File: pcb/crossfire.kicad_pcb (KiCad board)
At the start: 4 copper layers, 100 x 54 mm, 92 parts, among them J1 SWD+UART, J2 USB_A, J3 USB_A, J4 USB_A, J5 USB_A, J6 USB-C, SW1 BOOT, SW2 RESET, SW3 USER, U1 RP2350A, U10 TPS2065C, U11 USBLC6-2SC6, U12 USBLC6-2SC6, U14 AP63203WU, U2 W25Q128JVS, U3 USB2514B, U4 TPS2065C, U5 USBLC6-2SC6, U6 TPS2065C, U7 USBLC6-2SC6, U8 TPS2065C, U9 USBLC6-2SC6, Y1 12MHz, Y2 24MHz

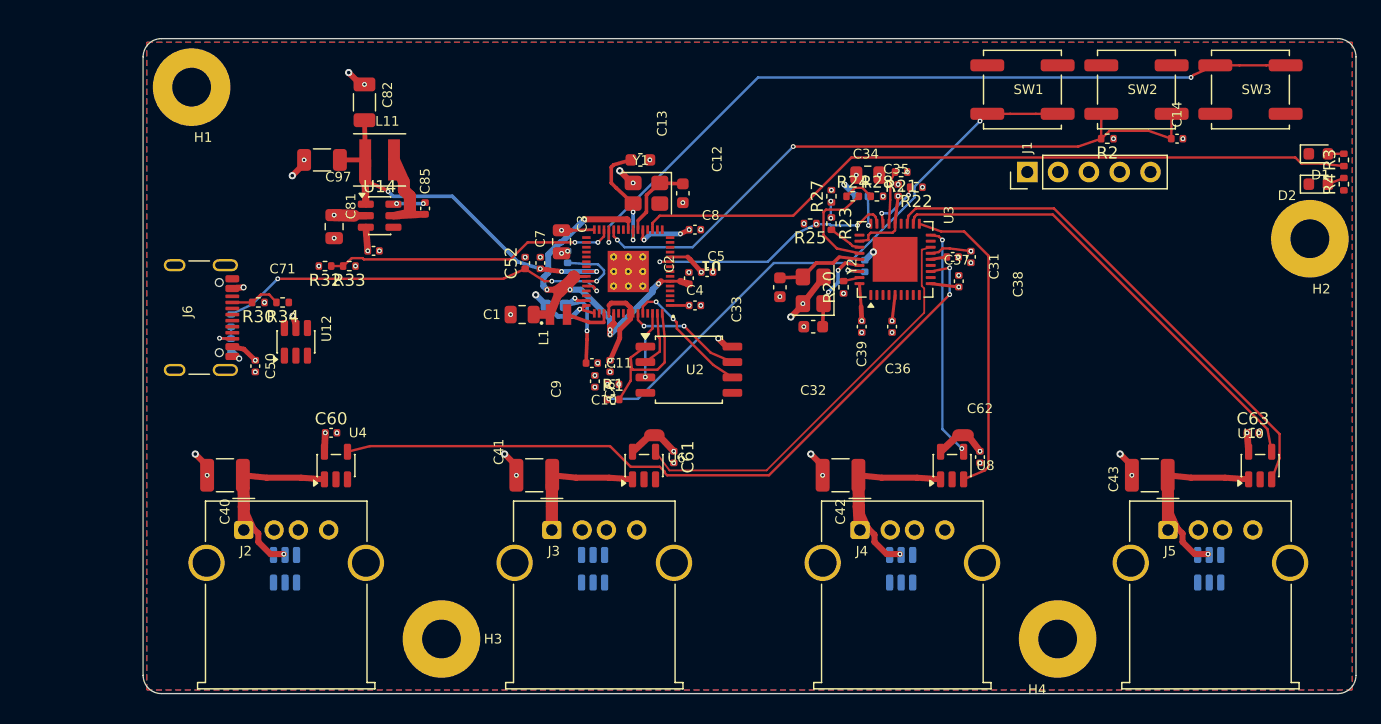
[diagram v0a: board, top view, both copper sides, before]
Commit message: hand layout and routing of the single-input board
All six pairs routed, the port power and fault lines moved to the back,
the crystal above the processor, a 100 nF on DVDD pin 23 added to the
schematic as C15. Rules check: three shorts on HUB_RESET's back-layer run
and three clearances still to clear; thirteen connections still open.

Co-Authored-By: Claude Fable 5.1 <noreply@anthropic.com>
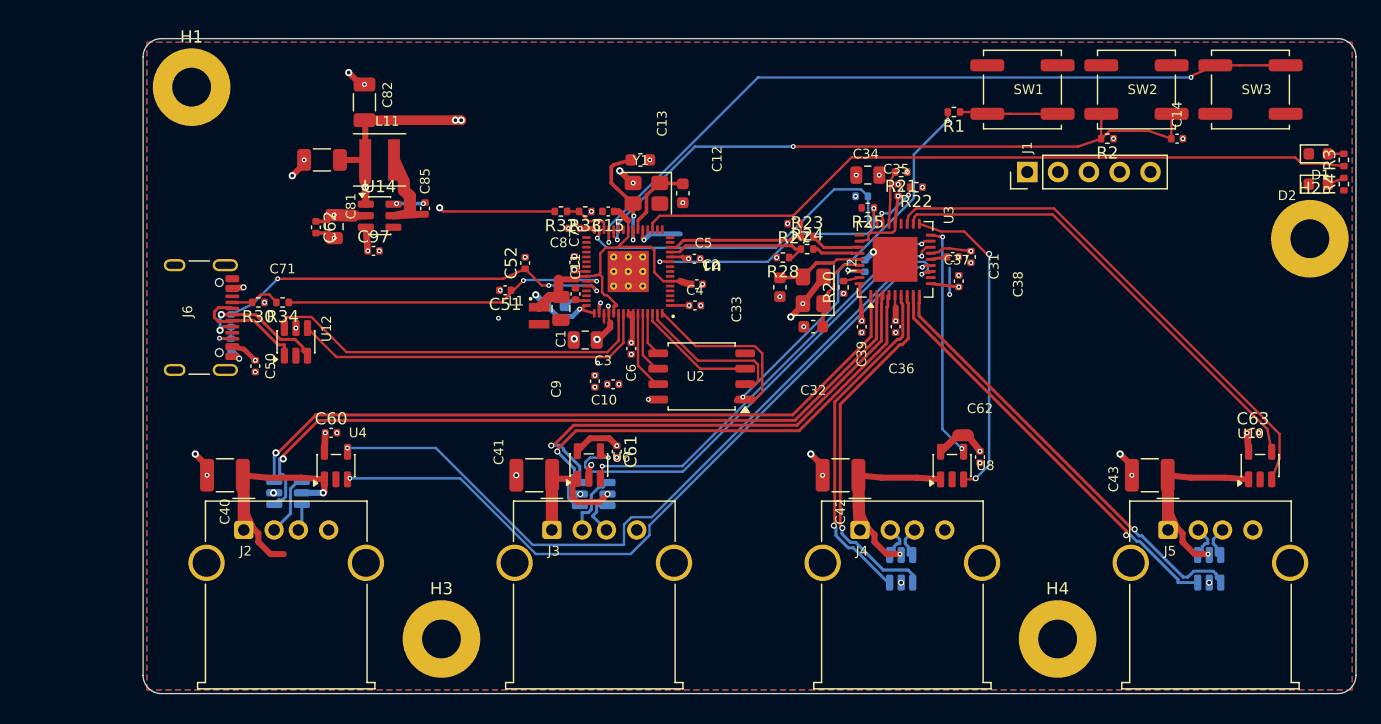
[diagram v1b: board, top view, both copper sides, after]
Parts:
- added C15: 100n, Capacitor_SMD:C_0402_1005Metric, F.Cu at (136.8, 59.2)
- added C62: 100n, Capacitor_SMD:C_0402_1005Metric, F.Cu at (112.8, 60.5)
- C51: footprint C_0402_1005Metric -> Capacitor_SMD:C_0402_1005Metric; moved to F.Cu
- C52, C60, C61, C63, C97: footprint C_0402_1005Metric -> Capacitor_SMD:C_0402_1005Metric
- H1, H2, H3, H4: footprint MountingHole_3.2mm_M3_Pad -> MountingHole:MountingHole_3.2mm_M3_Pad
- R1, R2, R20, R21, R22, R23, R24, R25, R26, R27, R28, R3, R30, R31, R32, R33, R34, R35, R4: footprint R_0402_1005Metric -> Resistor_SMD:R_0402_1005Metric
- U14: footprint TSOT-23-6 -> Package_TO_SOT_SMD:TSOT-23-6
- moved R1 36.8 mm to (165.3, 51.0), turned to 180 degrees
- moved R32 20.0 mm to (132.9, 59.2)
- moved R33 20.0 mm to (134.9, 59.2)
- moved C8 9.95 mm to (134.1, 60.6), turned to 180 degrees
- moved R28 9.25 mm to (151.2, 63.0), turned to 180 degrees
- moved C3 8.33 mm to (134.9, 69.8), turned to 180 degrees
- moved U5 6.26 mm to (110.5, 82.5), turned to 0 degrees
- moved U7 6.16 mm to (135.7, 82.5), turned to 0 degrees
- moved C11 5.86 mm to (134.2, 66.0), turned to 90 degrees
- moved C51 5.84 mm to (128.3, 65.8), turned to 180 degrees
- moved R24 5.74 mm to (153.2, 62.4)
- moved R25 4.92 mm to (158.2, 59.0)
- moved C61 4.72 mm to (137.6, 79.0)
- moved U6 4.55 mm to (135.2, 80.2)
- moved R27 3.83 mm to (152.2, 60.2), turned to 180 degrees
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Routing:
- net /P1_D+: track 0.00 -> 61.8 mm, vias 0 -> 1
- net /P1_OC: track 0.00 -> 61.0 mm, vias 0 -> 2
- net /P1_D-: track 0.00 -> 58.9 mm, vias 0 -> 1
- net /P2_D+: track 0.00 -> 41.0 mm, vias 0 -> 1
- net Net-(R1-Pad1): track 47.4 -> 8.10 mm, vias 2 -> 0
- net /P2_D-: track 0.00 -> 39.2 mm, vias 0 -> 1
- net /P4_D+: track 0.00 -> 36.4 mm, vias 0 -> 1
- net /P2_OC: track 0.00 -> 35.9 mm, vias 0 -> 2
- net /P4_D-: track 0.00 -> 34.8 mm, vias 0 -> 1
- net Net-(U1-~{QSPI_SS}): track 13.2 -> 45.8 mm, vias 0 -> 2
- net /USB_D-: track 0.00 -> 32.2 mm
- net /USB_D+: track 0.00 -> 30.5 mm
- net /P3_D+: track 0.00 -> 30.1 mm, vias 0 -> 1
- net /P3_D-: track 0.00 -> 28.5 mm, vias 0 -> 1
- net /HUB_VBUS_DET: track 2.64 -> 28.3 mm, vias 1 -> 2
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
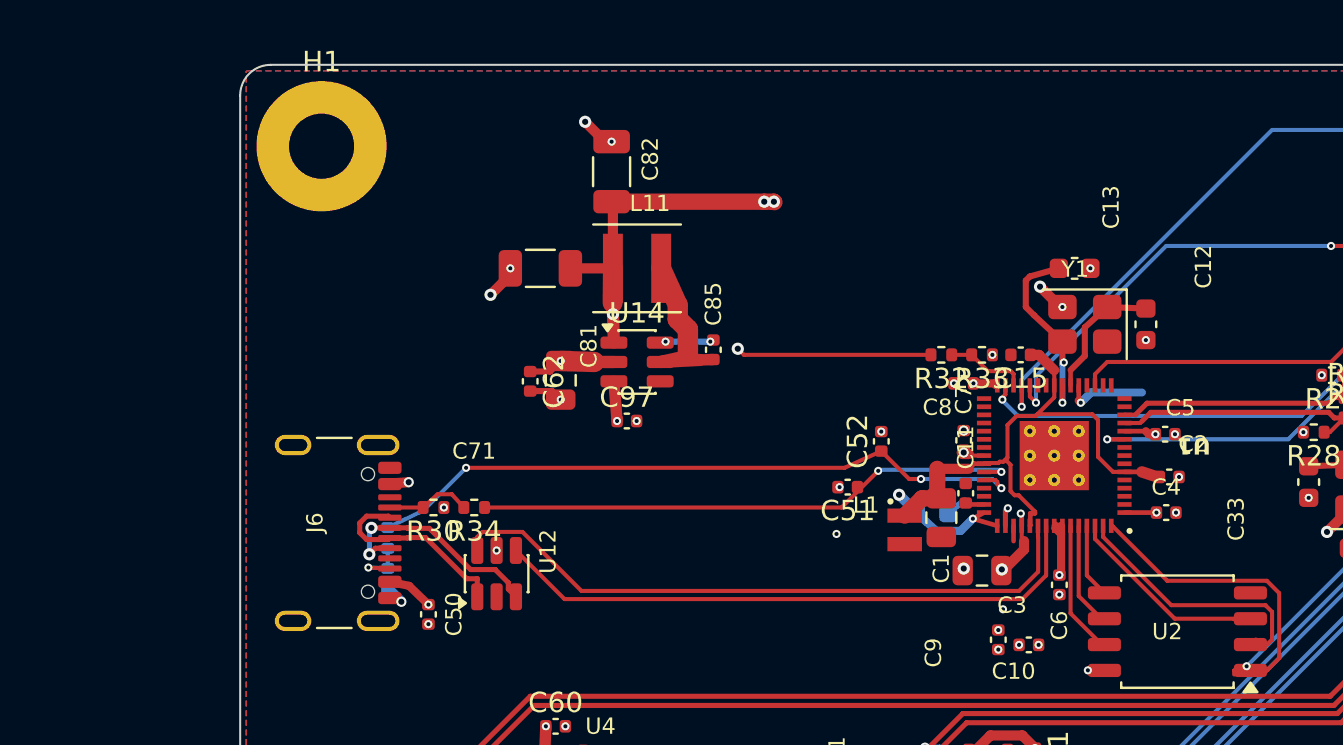
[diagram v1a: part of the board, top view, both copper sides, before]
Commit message: take the processor's regulator parts from the vendor's reference design
4.7 uF in 0402 on VREG_VIN and on the core rail, where this board had 10 uF
and 4.7 uF in 0805, and a 33 ohm / 4.7 uF filter on VREG_AVDD, which it
did not have at all. The crystal's load capacitors go to 0402 and the
3.3 V buck's capacitors to 0603. Footprints are swapped on the board in
place so the layout stands; R5 and C16 are parked outside the left edge.

Co-Authored-By: Claude Fable 5.1 <noreply@anthropic.com>
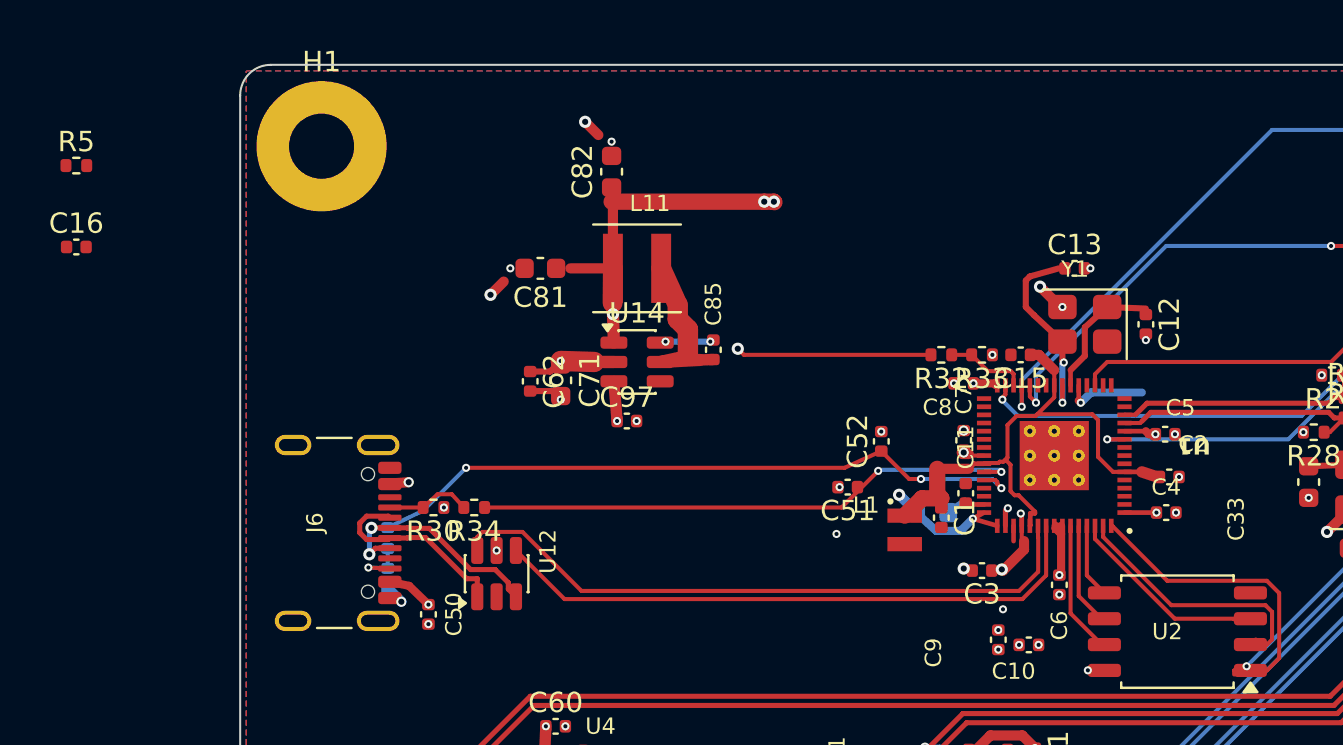
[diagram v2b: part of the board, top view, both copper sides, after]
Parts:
- added C16: 4u7, C_0402_1005Metric, F.Cu at (90.5, 54.0)
- added R5: 33R, R_0402_1005Metric, F.Cu at (90.5, 50.0)
- C1: footprint Capacitor_SMD:C_0805_2012Metric -> C_0402_1005Metric
- C12, C13: footprint Capacitor_SMD:C_0603_1608Metric -> C_0402_1005Metric
- C3: value 10u -> 4u7; footprint Capacitor_SMD:C_0805_2012Metric -> C_0402_1005Metric
- C71: footprint Capacitor_SMD:C_0805_2012Metric -> C_0603_1608Metric
- C81, C82: footprint Capacitor_SMD:C_1206_3216Metric -> C_0603_1608Metric

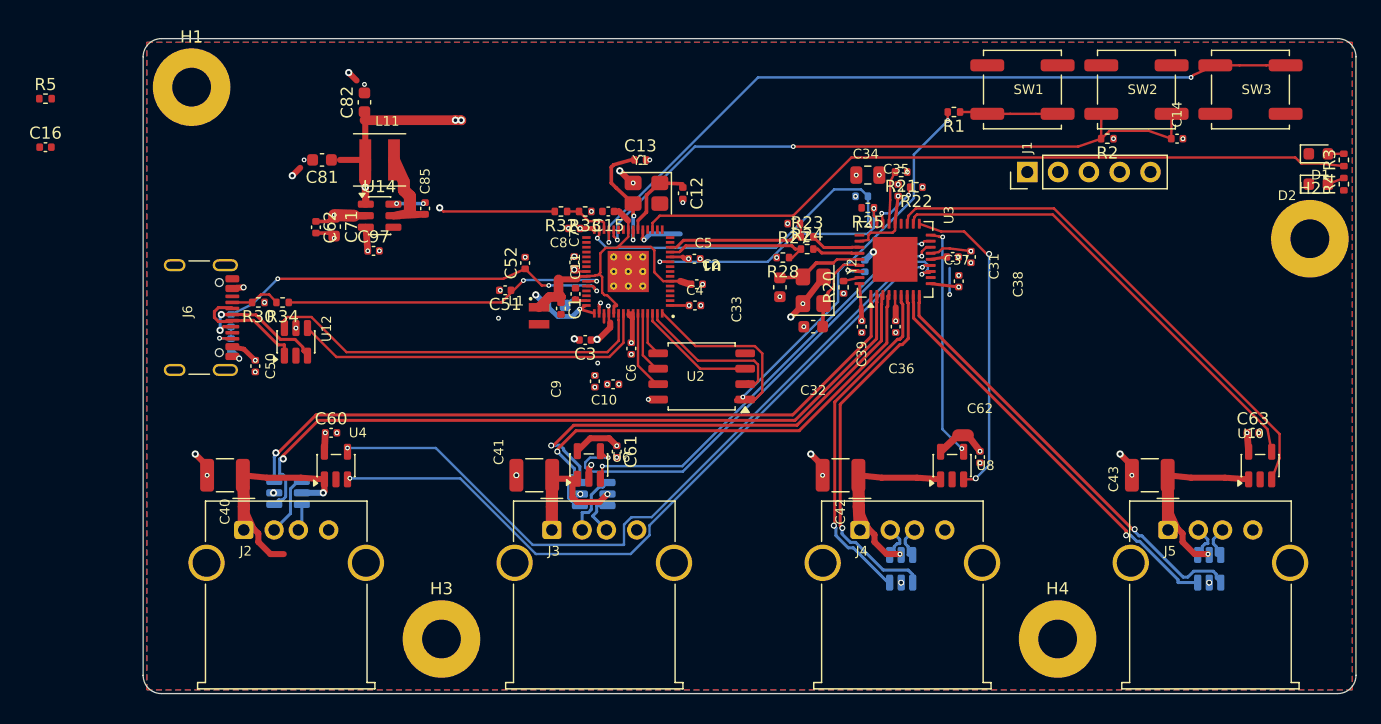
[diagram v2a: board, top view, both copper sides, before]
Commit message: footprints swapped by script carry their library name and their symbol's fields; the unlinked copy of C62 is removed; the VREG_AVDD filter's pads are on the net the schematic names
Co-Authored-By: Claude Fable 5.1 <noreply@anthropic.com>
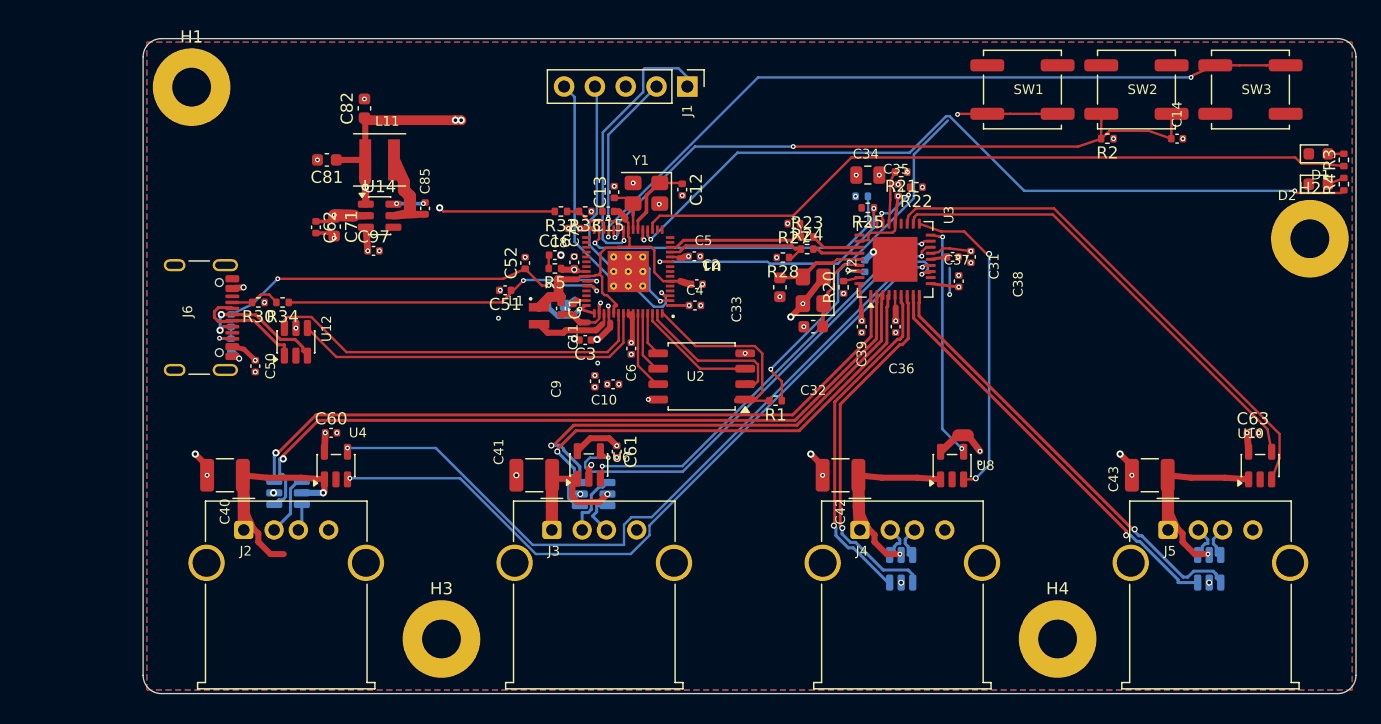
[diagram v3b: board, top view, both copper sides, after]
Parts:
- removed the C62 at (167.5, 79.5)
- C1, C12, C13, C16, C3: footprint C_0402_1005Metric -> Capacitor_SMD:C_0402_1005Metric
- C71, C81, C82: footprint C_0603_1608Metric -> Capacitor_SMD:C_0603_1608Metric
- R5: footprint R_0402_1005Metric -> Resistor_SMD:R_0402_1005Metric
- moved R5 44.3 mm to (132.4, 64.0), turned to 180 degrees
- moved C16 42.9 mm to (132.4, 62.9)
- moved J1 28.9 mm to (143.4, 49.0), turned to -90 degrees
- moved R1 28.0 mm to (150.7, 74.8)
- moved C13 3.41 mm to (137.3, 57.6), turned to 90 degrees
- moved C11 1.32 mm to (133.9, 67.3), turned to -90 degrees
- moved C82 0.50 mm to (116.8, 50.8)
- moved C81 0.40 mm to (113.7, 55.0)
- moved C12 0.30 mm to (142.9, 57.5)
- moved C5 0.20 mm to (143.9, 63.0)
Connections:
- C16 pad 1: Net-(R5-Pad2) -> Net-(U1-VREG_AVDD)
- R5 pad 2: Net-(R5-Pad2) -> Net-(U1-VREG_AVDD)
- U1 pad 46: +3V3 -> Net-(U1-VREG_AVDD)
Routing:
- net Net-(U1-GPIO15): track 0.00 -> 64.9 mm, vias 0 -> 2
- net Net-(R1-Pad1): track 8.10 -> 38.2 mm, vias 0 -> 2
- net Net-(U1-~{QSPI_SS}): track 45.8 -> 17.1 mm, vias 2 -> 0
- net /mcu/CONSOLE_RX: track 0.00 -> 25.1 mm, vias 0 -> 1
- net /mcu/CONSOLE_TX: track 0.00 -> 23.0 mm, vias 0 -> 1
- net Net-(J1-Pin_1): track 0.00 -> 23.0 mm, vias 0 -> 1
- net Net-(J1-Pin_2): track 0.00 -> 14.0 mm, vias 0 -> 1
- net Net-(U1-VREG_LX): track 0.75 -> 6.55 mm
- net Net-(U1-XOUT): track 9.45 -> 3.76 mm, vias 2 -> 0
- net +3V3: track 59.2 -> 56.1 mm, vias 23 -> 22
- net GND: track 14.5 -> 15.8 mm
- net Net-(U1-VREG_AVDD): track 0.00 -> 1.11 mm
- net /HUB_VBUS_DET: track 28.3 -> 27.4 mm
- net Net-(U1-GPIO16): track 63.5 -> 62.6 mm

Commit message: the analogue-supply filter as 100 ohms and 1 uF: the same corner, a smaller part, no 4 V rating
Co-Authored-By: Claude Fable 5.1 <noreply@anthropic.com>
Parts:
- C16: value 4u7 -> 1u
- FB1: moved to F.Cu
- R5: value 33R -> 100R
- moved C16 4.30 mm to (132.6, 67.2), turned to 180 degrees
- moved R5 2.10 mm to (132.6, 66.0), turned to 0 degrees
- moved C1 1.70 mm to (134.2, 68.3), turned to 0 degrees
- moved FB1 1.67 mm to (130.8, 66.8), turned to -90 degrees
- moved L1 1.64 mm to (132.2, 69.2), turned to 0 degrees
- moved C11 0.90 mm to (133.9, 66.5), turned to 90 degrees
- moved C3 0.40 mm to (135.3, 69.8)
- moved C7 0.10 mm to (134.2, 63.5)
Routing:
- net +1V1: track 28.7 -> 40.2 mm, vias 0 -> 2
- net +3V3: track 56.1 -> 50.8 mm, vias 22 -> 23
- net Net-(U1-VREG_AVDD): track 1.11 -> 3.87 mm
- net +3.3VA: track 2.22 -> 4.88 mm, vias 0 -> 2
- net Net-(U1-VREG_LX): track 6.55 -> 4.26 mm
- net /P1_PWR: track 66.0 -> 63.8 mm, vias 3 -> 2
- net /CC2_SENSE: track 33.2 -> 31.1 mm, vias 3 -> 1
- net GND: track 15.8 -> 14.0 mm, vias 63 -> 64
- net /CC1_SENSE: track 27.0 -> 25.4 mm
- net +5V: vias 10 -> 14
